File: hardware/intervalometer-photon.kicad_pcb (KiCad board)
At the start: 2 copper layers, 6 parts, among them J3 Conn_01x02, SW1 SW_DIP_x01, U1 LTV-827, U2 Photon

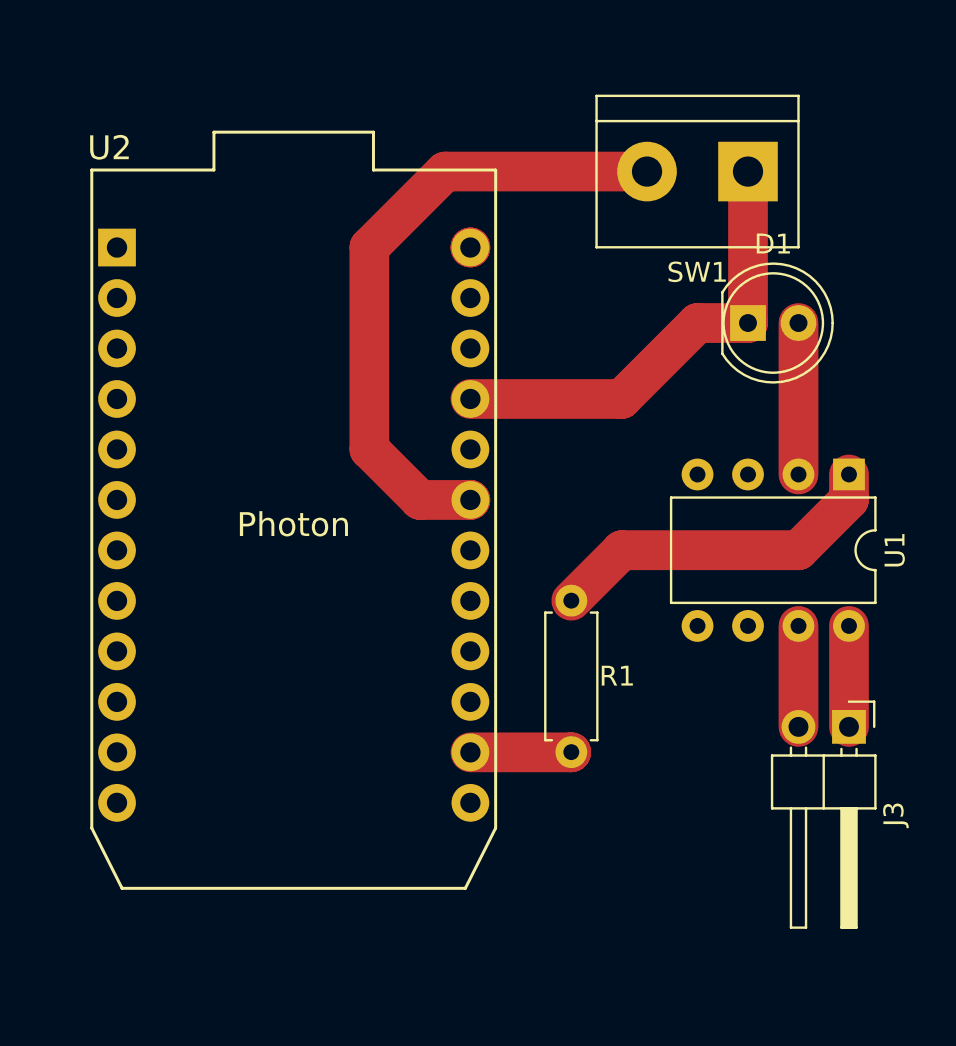
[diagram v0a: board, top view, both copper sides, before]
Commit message: Added support for switch to start / end activity
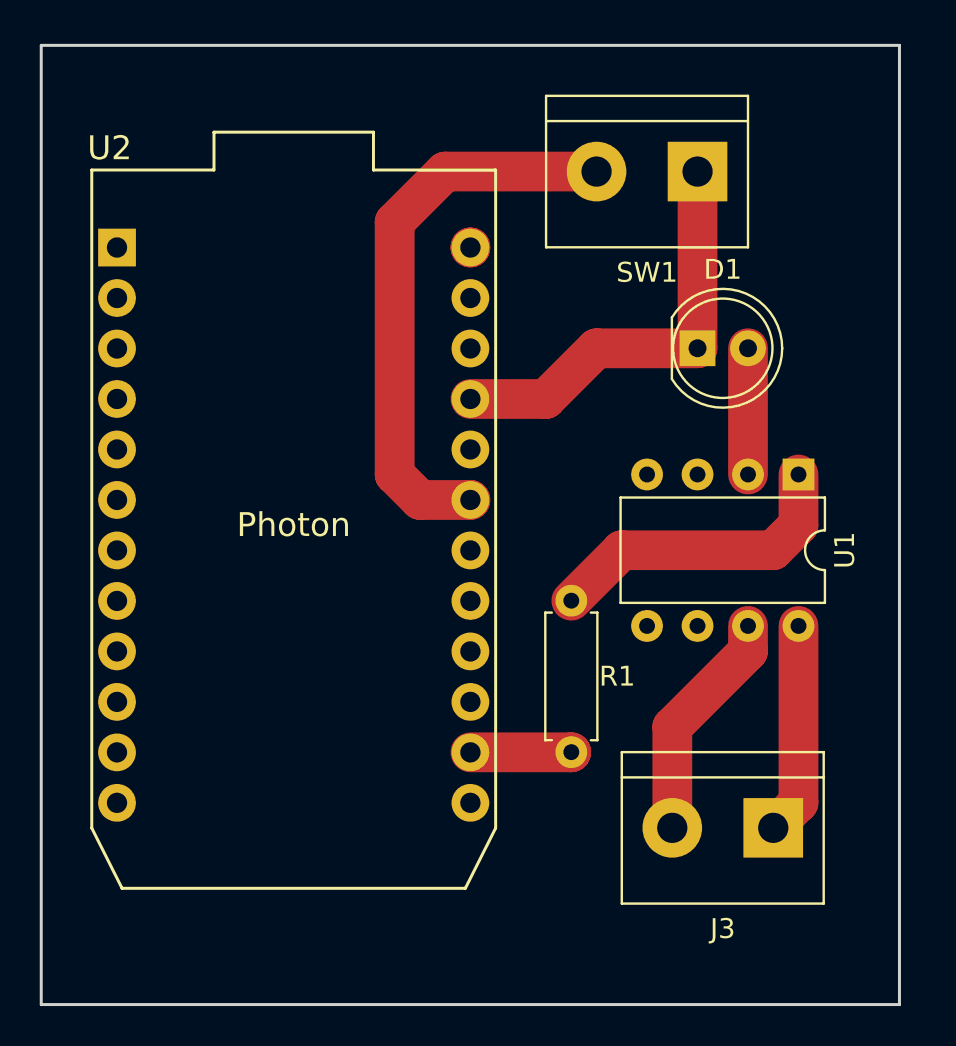
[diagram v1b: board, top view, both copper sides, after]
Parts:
- J3: footprint Pin_Headers:Pin_Header_Angled_1x02_Pitch2.54mm -> Connectors_Terminal_Blocks:TerminalBlock_bornier-2_P5.08mm
- moved J3 6.35 mm to (179.1, 129.5), turned to 180 degrees
- moved D1 2.84 mm to (175.3, 105.4)
- moved SW1 2.54 mm to (175.3, 96.5)
- moved U1 2.54 mm to (180.3, 111.8)
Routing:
- net Net-(J3-Pad2): track 5.08 -> 11.7 mm
- net Net-(J3-Pad1): track 5.08 -> 10.7 mm
- net START: track 31.9 -> 28.3 mm
- net GND: track 23.2 -> 21.4 mm
- net Net-(R1-Pad1): track 17.3 -> 15.5 mm
- net Net-(D1-Pad2): track 7.62 -> 6.35 mm
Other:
- board outline added: 43.2 x 48.3 mm

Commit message: updated hardware schematics
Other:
- board text added: "Switch"
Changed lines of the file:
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@@
     (area 142.164999 90.094999 185.495001 138.505001)
     (thickness 1.6)
-    (drawings 4)
+    (drawings 5)
     (tracks 24)
     (zones 0)
@@
     )
   )
+  (gr_text Switch (at 172.72 91.44) (layer F.SilkS)
+    (effects (font (size 1.5 1.5) (thickness 0.3)))
+  )
   (gr_line (start 142.24 138.43) (end 142.24 90.17) (angle 90) (layer Edge.Cuts) (width 0.15))
   (gr_line (start 185.42 138.43) (end 142.24 138.43) (angle 90) (layer Edge.Cuts) (width 0.15))
   (gr_line (start 185.42 90.17) (end 185.42 138.43) (angle 90) (layer Edge.Cuts) (width 0.15))
   (gr_line (start 142.24 90.17) (end 185.42 90.17) (angle 90) (layer Edge.Cuts) (width 0.15))
-  (segment (start 175.26 105.41) (end 175.26 96.52) (width 2) (layer F.Cu) (net 1) (status C00000))
-  (segment (start 163.83254 107.96172) (end 167.62828 107.96172) (width 2) (layer F.Cu) (net 1) (status 400000))
-  (segment (start 170.18 105.41) (end 175.26 105.41) (width 2) (layer F.Cu) (net 1) (status 800000))
+  (segment (start 175.26 105.41) (end 175.26 96.52) (width 2) (layer F.Cu) (net 1))
+  (segment (start 163.83254 107.96172) (end 167.62828 107.96172) (width 2) (layer F.Cu) (net 1))
+  (segment (start 170.18 105.41) (end 175.26 105.41) (width 2) (layer F.Cu) (net 1))
   (segment (start 167.62828 107.96172) (end 170.18 105.41) (width 2) (layer F.Cu) (net 1))
-  (segment (start 177.8 111.76) (end 177.8 105.41) (width 2) (layer F.Cu) (net 2) (status C00000))
+  (segment (start 177.8 111.76) (end 177.8 105.41) (width 2) (layer F.Cu) (net 2))
   (segment (start 163.83254 125.74172) (end 168.89828 125.74172) (width 2) (layer F.Cu) (net 3))
   (segment (start 168.89828 125.74172) (end 168.91 125.73) (width 2) (layer F.Cu) (net 3))
